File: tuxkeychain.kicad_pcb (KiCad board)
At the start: 4 copper layers, 50 x 60 mm, 54 parts, among them J1 Amphenol_10104111, J3 EXPANSION, J5 Solder Pads, Q2 2N7002, SW1 B3U-1000P, U4 F1C100s, U5 TLV76701DRVx, U6 W25Q128JVS, U7 TLV76701DRVx, U8 TLV76701DRVx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

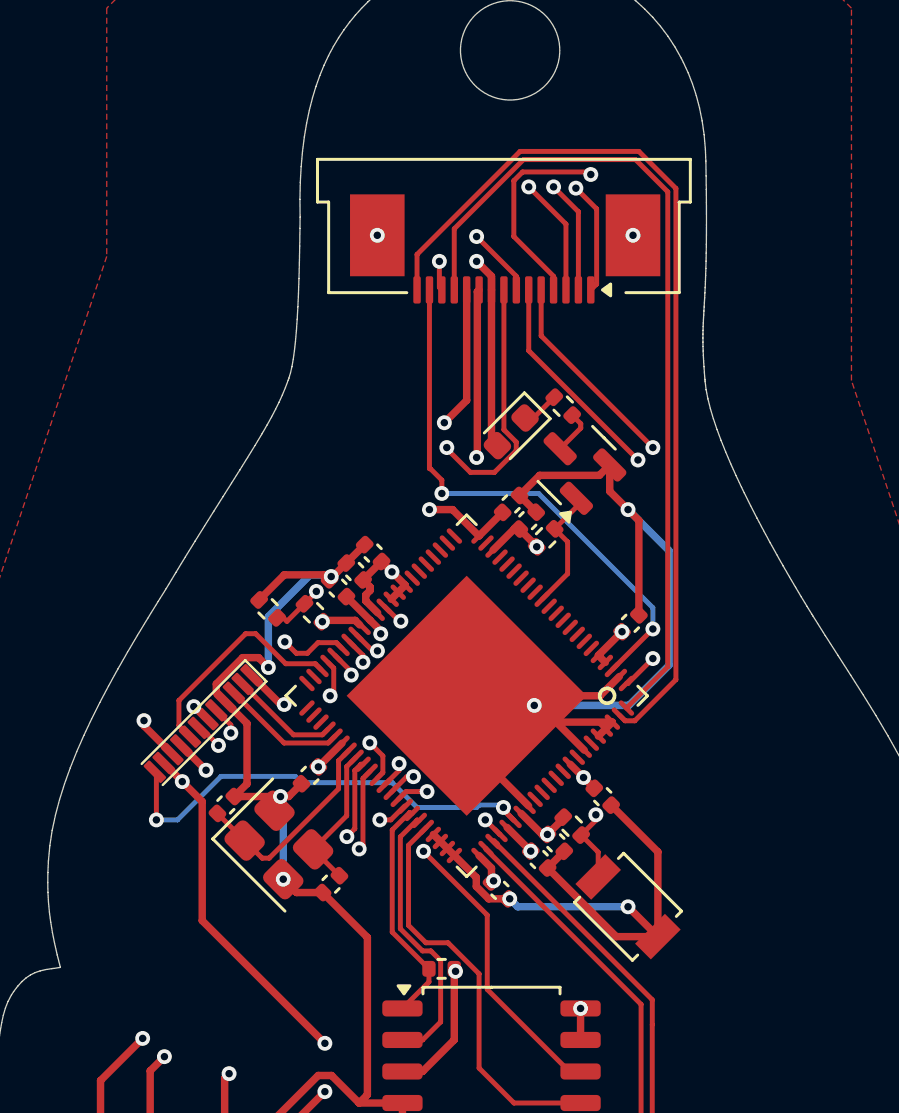
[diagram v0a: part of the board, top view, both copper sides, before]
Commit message: Changed board to 6 layers, made appropriate routing changes
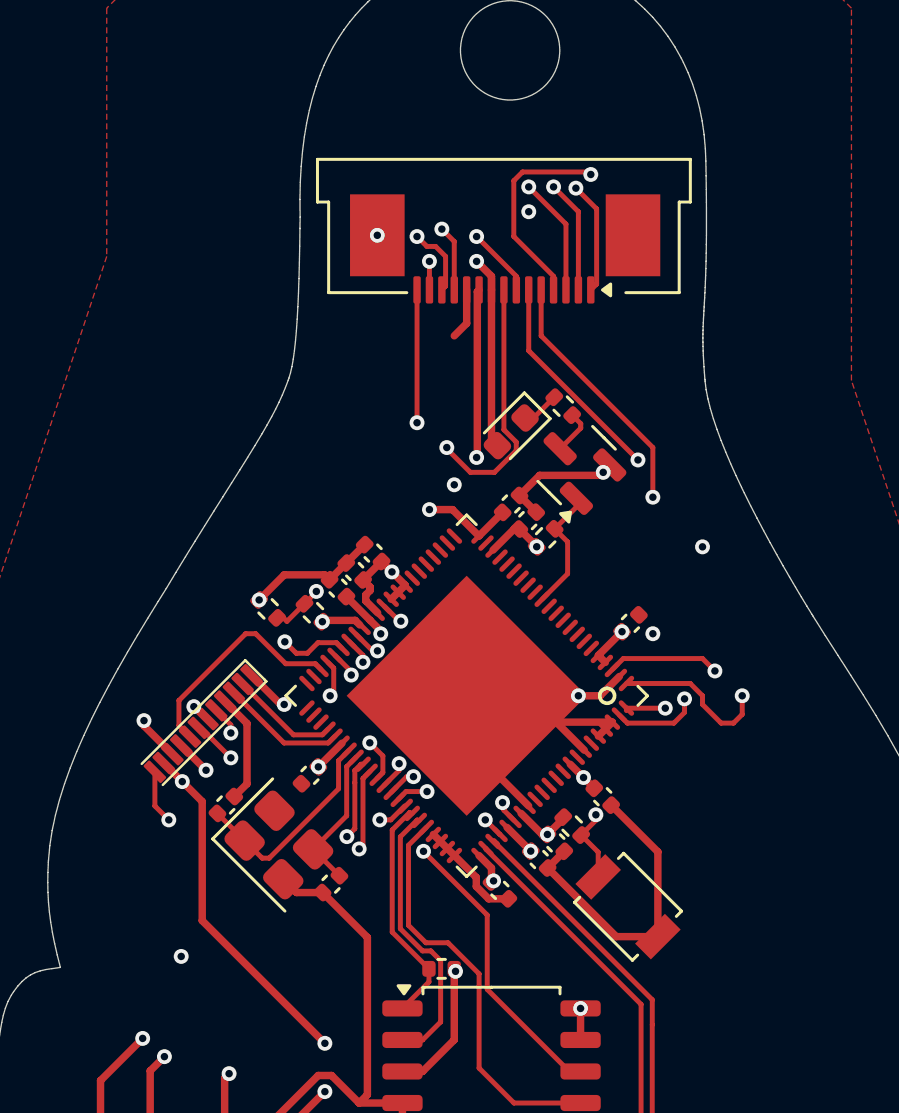
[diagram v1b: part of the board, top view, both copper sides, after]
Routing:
- net GND: track 253.3 -> 140.2 mm, vias 11 -> 9
- net MICIN: track 37.0 -> 26.2 mm, vias 0 -> 2
- net HPCOM: track 22.0 -> 26.9 mm
- net SDC0_D1/JTAG_TMS: track 30.3 -> 27.8 mm
- net SDC0_CLK: track 36.4 -> 38.6 mm
- net TVOUT: track 18.7 -> 17.1 mm
- net HPL: track 32.7 -> 33.9 mm
- net HPR: track 34.2 -> 33.9 mm, vias 0 -> 2
- added copper zone on In3.Cu, net GND
- added copper zone on In4.Cu, net GND
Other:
- copper layers 4 -> 6

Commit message: minor trace cleanups
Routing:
- net HPL: track 33.9 -> 32.3 mm
- net +5V: track 65.9 -> 65.3 mm
- net GND: vias 9 -> 13
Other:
- board text added: "Εδέμ Was Here"
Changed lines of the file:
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@@
 		)
 		(property "Value" "Solder Pads"
-			(at 0 7.5 225)
+			(at -0.871321 2.12132 225)
 			(unlocked yes)
 			(layer "F.Fab")
@@
 		)
 		(fp_text user "${REFERENCE}"
-			(at 0 9 225)
+			(at -0.871321 -1.414214 225)
 			(unlocked yes)
 			(layer "F.Fab")
@@
 		)
 	)
+	(gr_text "Εδέμ Was Here"
+		(at 12 197.7 0)
+		(layer "Cmts.User")
+		(effects
+			(font
+				(size 3 3)
+				(thickness 0.6)
+				(bold yes)
+			)
+			(justify left bottom)
+		)
+	)
 	(gr_text "Tux is 60x50mm"
 		(locked yes)
@@
 	)
 	(segment
-		(start 106.571345 83.7)
-		(end 104.5 83.7)
-		(width 0.3)
-		(layer "In1.Cu")
-		(net 1)
-	)
-	(segment
-		(start 110.5 80.7)
-		(end 109.571345 80.7)
+		(start 104.5 83.7)
+		(end 106.571345 83.7)
 		(width 0.3)
 		(layer "In1.Cu")
@@
 	)
 	(segment
-		(start 104.5 83.7)
-		(end 101.5 86.7)
+		(start 106.571345 83.7)
+		(end 112.5 77.771345)
 		(width 0.3)
 		(layer "In1.Cu")
@@
 	)
 	(segment
-		(start 101.5 85.2)
-		(end 101 84.7)
+		(start 112.5 77.771345)
+		(end 112.5 77.2)
 		(width 0.3)
 		(layer "In1.Cu")
@@
 	)
 	(segment
-		(start 112.5 72.7)
-		(end 112.5 78.7)
+		(start 101.5 85.2)
+		(end 101 84.7)
 		(width 0.3)
 		(layer "In1.Cu")
@@
 	)
 	(segment
-		(start 109.571345 80.7)
-		(end 106.571345 83.7)
+		(start 98.447343 95.502657)
+		(end 101.5 92.45)
 		(width 0.3)
 		(layer "In1.Cu")
@@
 	)
 	(segment
-		(start 98.447343 95.502657)
-		(end 101.5 92.45)
+		(start 112.5 72.7)
+		(end 112.5 77.2)
 		(width 0.3)
 		(layer "In1.Cu")
@@
 	)
 	(segment
-		(start 112.5 78.7)
-		(end 110.5 80.7)
+		(start 101.5 86.7)
+		(end 104.5 83.7)
 		(width 0.3)
 		(layer "In1.Cu")
@@
 	)
 	(via
+		(at 120 101.7)
+		(size 0.6)
+		(drill 0.3)
+		(layers "F.Cu" "B.Cu")
+		(free yes)
+		(net 2)
+	)
+	(via
 		(at 114 62.2)
 		(size 0.6)
@@
 	)
 	(via
+		(at 111 90.7)
+		(size 0.6)
+		(drill 0.3)
+		(layers "F.Cu" "B.Cu")
+		(free yes)
+		(net 2)
+	)
+	(via
+		(at 113.5 96.7)
+		(size 0.6)
+		(drill 0.3)
+		(layers "F.Cu" "B.Cu")
+		(free yes)
+		(net 2)
+	)
+	(via
 		(at 116 81.7)
 		(size 0.6)
@@
 		(net 2)
 	)
+	(via
+		(at 126.5 93.2)
+		(size 0.6)
+		(drill 0.3)
+		(layers "F.Cu" "B.Cu")
+		(free yes)
+		(net 2)
+	)
 	(segment
 		(start 98.75 99.325002)
@@
 	)
 	(segment
-		(start 119.601 75.861741)
-		(end 109.903923 85.558818)
+		(start 110.012661 85.45008)
+		(end 110.012661 84.71266)
+		(width 0.2)
+		(layer "In1.Cu")
+		(net 35)
+	)
+	(segment
+		(start 119.601 75.124321)
+		(end 119.601 74.2)
 		(width 0.2)
 		(layer "In1.Cu")
@@
 	(segment
 		(start 119.601 73.401)
-		(end 119.601 75.861741)
+		(end 119.601 74.2)
+		(width 0.2)
+		(layer "In1.Cu")
+		(net 35)
+	)
+	(segment
+		(start 109.903923 85.558818)
+		(end 110.012661 85.45008)
+		(width 0.2)
+		(layer "In1.Cu")
+		(net 35)
+	)
+	(segment
+		(start 110.012661 84.71266)
+		(end 119.601 75.124321)
 		(width 0.2)
 		(layer "In1.Cu")
@@
 	)
 	(segment
-		(start 121 81.7)
-		(end 121 82.049943)
-		(width 0.2)
-		(layer "F.Cu")
-		(net 58)
-	)
-	(segment
-		(start 122.248943 82.801)
-		(end 122.6 82.449943)
-		(width 0.2)
-		(layer "F.Cu")
-		(net 58)
-	)
-	(segment
-		(start 120.505025 81.205025)
+		(start 122.6 81.7)
 		(end 121 81.7)
 		(width 0.2)
@@
 	)
 	(segment
-		(start 121.751057 82.801)
-		(end 122.248943 82.801)
-		(width 0.2)
-		(layer "F.Cu")
-		(net 58)
-	)
-	(segment
-		(start 121 82.049943)
-		(end 121.751057 82.801)
-		(width 0.2)
-		(layer "F.Cu")
-		(net 58)
-	)
-	(segment
 		(start 109.899 63.599)
 		(end 109.5 63.2)
@@
 	)
 	(segment
-		(start 122.6 82.449943)
-		(end 122.6 81.7)
-		(width 0.2)
-		(layer "F.Cu")
-		(net 58)
-	)
-	(segment
 		(start 110.248943 63.599)
 		(end 109.899 63.599)
@@
 		(net 58)
 	)
+	(segment
+		(start 121 81.7)
+		(end 120.505025 81.205025)
+		(width 0.2)
+		(layer "F.Cu")
+		(net 58)
+	)
 	(via
 		(at 122.6 81.7)
@@
 	)
 	(segment
-		(start 118.560043 74.260043)
-		(end 118 73.7)
+		(start 109.010261 84.2)
+		(end 108.777683 84.432578)
 		(width 0.2)
 		(layer "In1.Cu")
@@
 	)
 	(segment
-		(start 118 72.7)
-		(end 117.601 72.301)
+		(start 118.560043 74.260043)
+		(end 118 73.7)
 		(width 0.2)
 		(layer "In1.Cu")
@@
 	)
 	(segment
-		(start 108.777683 84.432578)
-		(end 116.5 76.710261)
+		(start 118 73.7)
+		(end 118 72.7)
 		(width 0.2)
 		(layer "In1.Cu")
@@
 	)
 	(segment
-		(start 116.5 76.710261)
-		(end 116.989739 76.710261)
+		(start 117.601 72.301)
+		(end 117.601 61.801)
 		(width 0.2)
 		(layer "In1.Cu")
@@
 	)
 	(segment
-		(start 117.601 72.301)
-		(end 117.601 61.801)
+		(start 118.7101 74.9899)
+		(end 118.7101 74.260043)
 		(width 0.2)
 		(layer "In1.Cu")
@@
 	)
 	(segment
-		(start 118 73.7)
-		(end 118 72.7)
+		(start 109.5 84.2)
+		(end 118.7101 74.9899)
 		(width 0.2)
 		(layer "In1.Cu")
@@
 	)
 	(segment
-		(start 118.7101 74.9899)
-		(end 118.7101 74.260043)
+		(start 118 72.7)
+		(end 117.601 72.301)
 		(width 0.2)
 		(layer "In1.Cu")
@@
 	)
 	(segment
-		(start 116.989739 76.710261)
-		(end 118.7101 74.9899)
+		(start 109.5 84.2)
+		(end 109.010261 84.2)
 		(width 0.2)
 		(layer "In1.Cu")

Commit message: fix drc
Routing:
- net GND: track 140.2 -> 140.9 mm, vias 13 -> 14
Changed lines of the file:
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@@
+	)
+	(segment
+		(start 104.771262 85.242605)
+		(end 104.323948 84.795291)
+		(width 0.3)
+		(layer "F.Cu")
+		(net 2)
 	)
 	(segment
@@
 	)
 	(segment
+		(start 104.846125 85.242605)
+		(end 104.771262 85.242605)
+		(width 0.3)
+		(layer "F.Cu")
+		(net 2)
+	)
+	(segment
 		(start 114.045584 81.7)
 		(end 111.5 81.7)
@@
 		(size 0.6)
 		(drill 0.3)
+		(layers "F.Cu" "B.Cu")
+		(net 2)
+	)
+	(via
+		(at 104.323948 84.795291)
+		(size 0.6)
+		(drill 0.3)

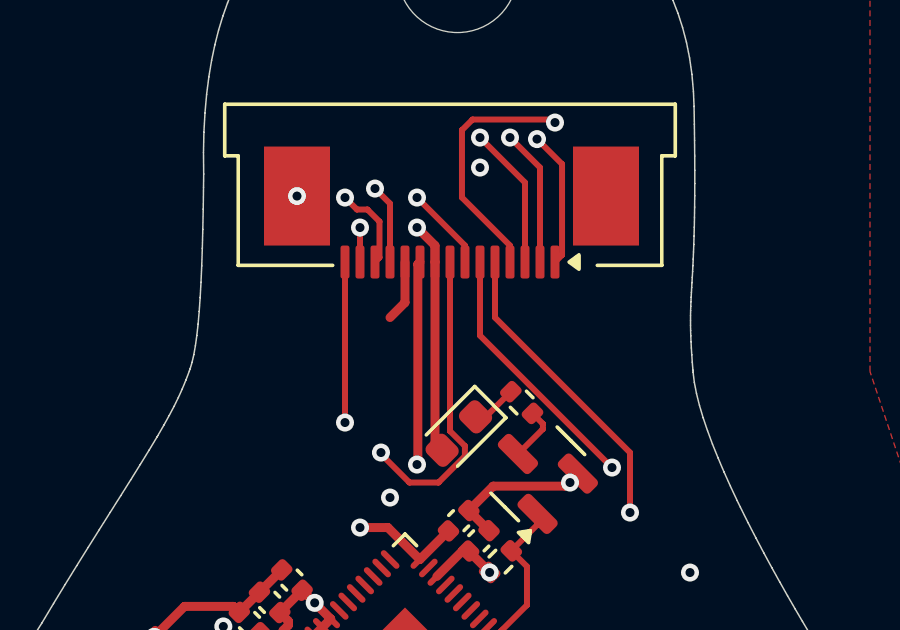
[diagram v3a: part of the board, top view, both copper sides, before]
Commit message: fix name for footprint
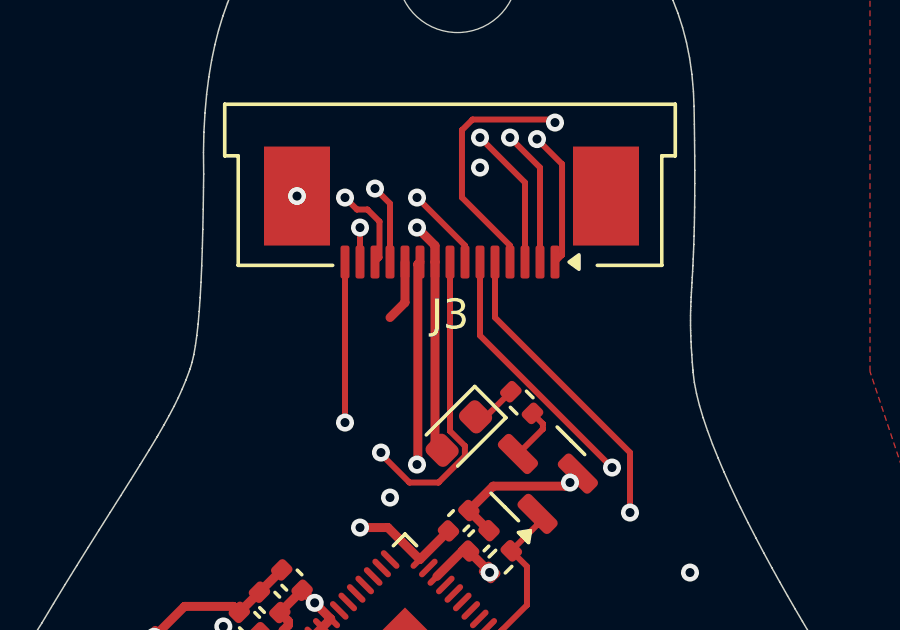
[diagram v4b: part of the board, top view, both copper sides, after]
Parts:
- J3: footprint tuxkeychain:FFC_1x15_P0.5mm -> tuxkeychain:Jushuo_AFC07-S15FCA-00_1x15-1MP_P0.50_Horizontal
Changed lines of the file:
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@@
 		)
 	)
-	(footprint "tuxkeychain:FFC_1x15_P0.5mm"
+	(footprint "tuxkeychain:Jushuo_AFC07-S15FCA-00_1x15-1MP_P0.50_Horizontal"
 		(locked yes)
 		(layer "F.Cu")
@@
 		(tags "F32T")
 		(property "Reference" "J3"
-			(at 0 -4.65 0)
-			(layer "F.SilkS")
-			(hide yes)
+			(at 0 -4.65 180)
+			(layer "F.SilkS")
 			(effects
 				(font
@@
 		)
 		(property "Value" "EXPANSION"
-			(at 0 3.45 0)
+			(at 0 3.45 180)
 			(layer "F.Fab")
 			(effects
@@
 		)
 		(property "Datasheet" ""
-			(at 0 0 0)
+			(at 0 0 180)
 			(layer "F.Fab")
 			(hide yes)
@@
 			)
 		)
-		(property "Description" "Generic connectable mounting pin connector, single row, 01x15, script generated (kicad-library-utils/schlib/autogen/connector/)"
-			(at 0 0 0)
+		(property "Description" ""
+			(at 0 0 180)
 			(layer "F.Fab")
 			(hide yes)
@@
 		)
 		(fp_text user "${REFERENCE}"
-			(at 0 0 0)
+			(at 0 0 180)
 			(layer "F.Fab")
 			(effects
@@
 		(model "${KICAD9_3DMODEL_DIR}/Connector_FFC-FPC.3dshapes/Hirose_FH12-15S-0.5SH_1x15-1MP_P0.50mm_Horizontal.wrl"
 			(offset
-				(xyz 0 1.5 0)
+				(xyz 0 0 0)
 			)
 			(scale
@@
 			)
 			(rotate
-				(xyz -0 -0 -0)
+				(xyz 0 0 0)
 			)
 		)
@@
 		(sheetname "/Expansion Connectors/")
 		(sheetfile "expansion.kicad_sch")
-		(attr smd)
+		(attr smd exclude_from_pos_files exclude_from_bom)
 		(fp_line
 			(start -3 0.6)
